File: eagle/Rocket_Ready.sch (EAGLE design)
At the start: 18 parts, among them IC1 HEX_INV_SHMITT_TRIG, IC2 OPTOISOLATOR, Q1 NMOSFET

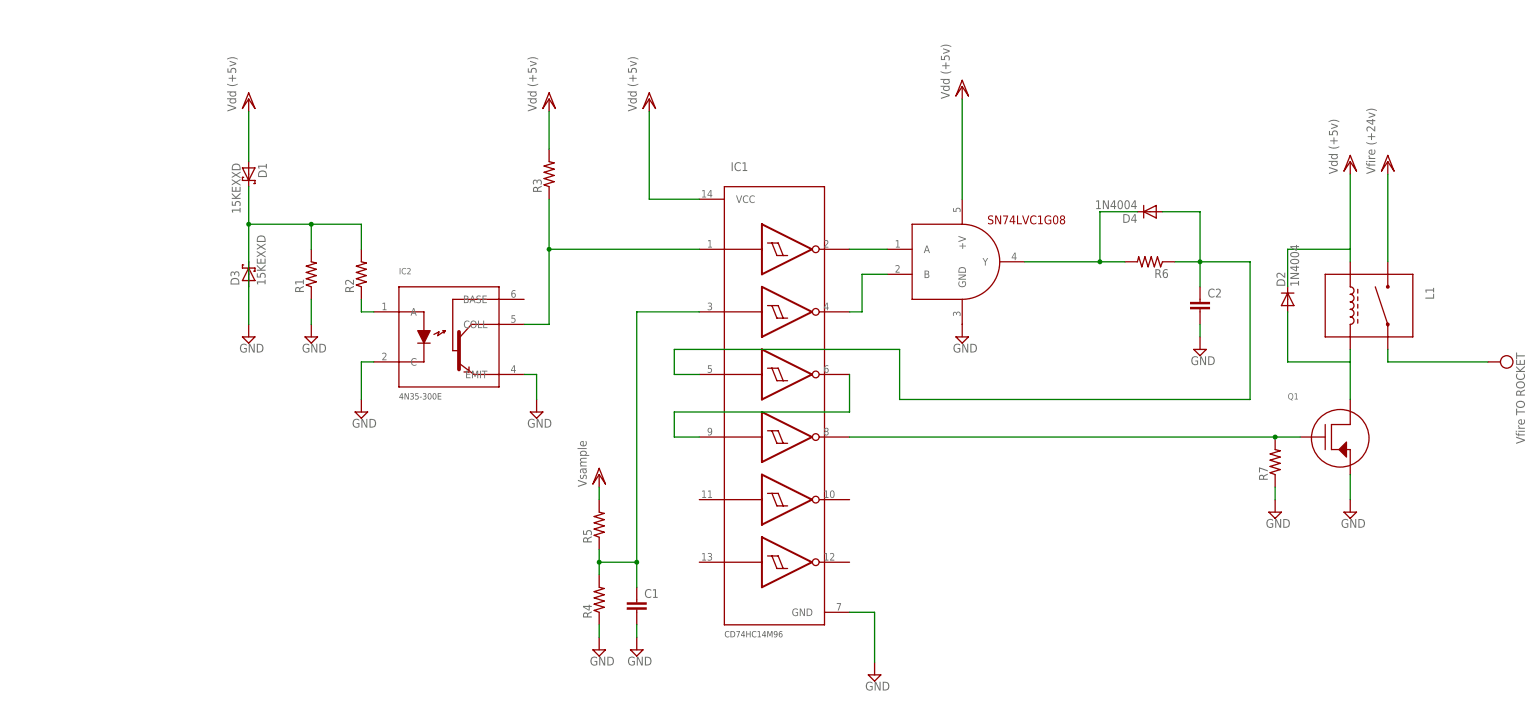
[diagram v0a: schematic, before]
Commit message: Updated schematic file (with nets) and board layout.
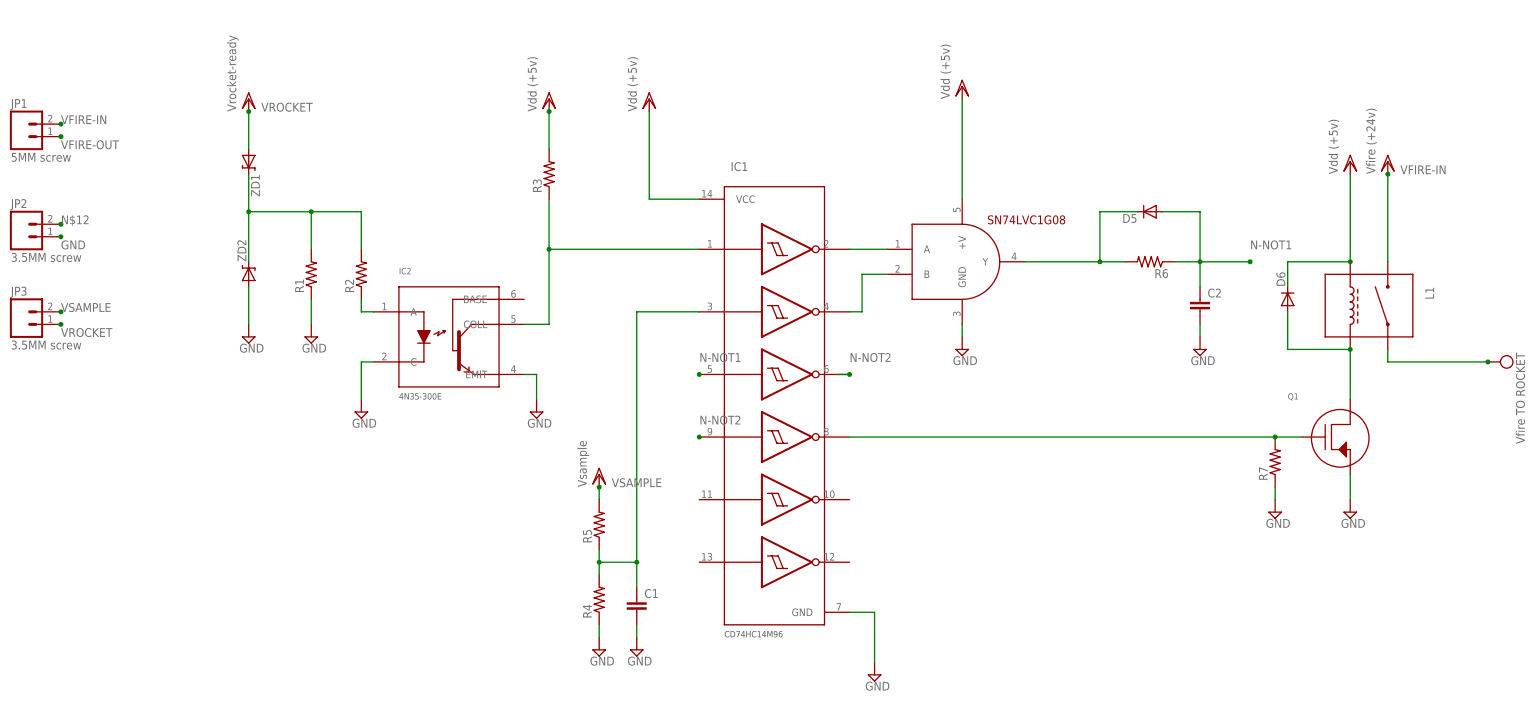
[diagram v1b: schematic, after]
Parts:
- removed D1, D3: 15KEXXD, launch-tower:15KEXXD
- removed D2, D4: 1N4004, launch-tower:1N4004
- added D5, D6: (no value), SparkFun:DIODEPTH
- added JP1: 5MM screw, SparkFun:M025MM
- added JP2, JP3: 3.5MM screw, SparkFun:M023.5MM
- added ZD1, ZD2: DIODE-ZENERPTH, SparkFun:DIODE-ZENERPTH
- IC1: value HEX_INV_SHMITT_TRIG -> INVERT GATES
- L1: value (none) -> RELAY
- U$1: value SN74LVC1G08 -> AND GATE
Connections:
- net N$10 renamed N-NOT2
- removed net N$1 (its old number): D2.A, L1.CIN, Q1.DRAIN
- removed net N$13: D4.C, R6.2, U$1.Y
- removed net VDD: D1.A, D2.C, IC1.VCC, L1.COUT, L1.SW1, L1.SW2, R3.2, R5.2, U$1.+V
- new net N$2: D5.C, R6.2, U$1.Y
- new net N$8: R1.2, R2.2, ZD1.C, ZD2.C
- new net N$9: D6.A, L1.CIN, Q1.DRAIN
- new net N-NOT1: C2.1, D5.A, IC1.3A, R6.1
- new net VFIRE-IN: JP1.2, L1.SW2
- new net VFIRE-OUT: JP1.1, L1.SW1
- new net VROCKET: JP3.1, ZD1.A
- new net VSAMPLE: JP3.2, R5.2
- net GND: now also JP2.1, ZD2.A; no longer D1.C, D3.A, D3.C, R1.2, R2.2
- net N$12: now also D6.C, IC1.VCC, JP2.2, L1.COUT, R3.2, U$1.+V; no longer C2.1, D4.A, IC1.3A, R6.1
